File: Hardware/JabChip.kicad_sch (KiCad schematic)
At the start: 44 parts, among them J1 USB_C, J2 JSTPH, J3 Piezo+, J4 Piezo-, SW1 434133025816, SW2 434133025816, U1 AP2112K-3.3, U2 MCP73831-2-OT, U3 LSM6DS3, U4 ESP32-S3-WROOM-1

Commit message: style: Clean up schematic
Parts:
- D4: value LED -> LED_R
- D7: value LED -> LED_G
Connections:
- net +5V: now also C3.2; no longer C3.1
- net GND: now also C3.1; no longer C3.2
- no-connect marks 10 -> 8
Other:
- note added: "SENSORS"
- note removed: "IMU"
- moved on the sheet: C13, C3, J3, J4, R10, R11, R12, U3

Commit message: fix: Reassign piezo from IO3 to IO9 to avoid JTAG debug
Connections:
- net 9 is gone; now on net Piezo: U4.17 (IO9)
- net Piezo: no longer U4.15 (IO3)
- new net 3: U4.15 (IO3)
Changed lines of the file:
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@@
+		)
+	)
+	(global_label "Piezo"
+		(shape input)
+		(at 35.56 132.08 180)
+		(fields_autoplaced yes)
+		(effects
+			(font
+				(size 1.27 1.27)
+			)
+			(justify right)
+		)
+		(property "Intersheetrefs" "${INTERSHEET_REFS}"
+			(at 27.4343 132.08 0)
+			(effects
+				(font
+					(size 1.27 1.27)
+				)
+				(justify right)
+				(hide yes)
+			)
 		)
 	)
@@
 				(hide yes)
 			)
-		)
-	)
-	(global_label "Piezo"
-		(shape input)
-		(at 35.56 116.84 180)
-		(fields_autoplaced yes)
-		(effects
-			(font
-				(size 1.27 1.27)
-			)
-			(justify right)
-		)
-		(property "Intersheetrefs" "${INTERSHEET_REFS}"
-			(at 27.4343 116.84 0)
-			(effects
-				(font
-					(size 1.27 1.27)
-				)
-				(justify right)
-				(hide yes)
-			)

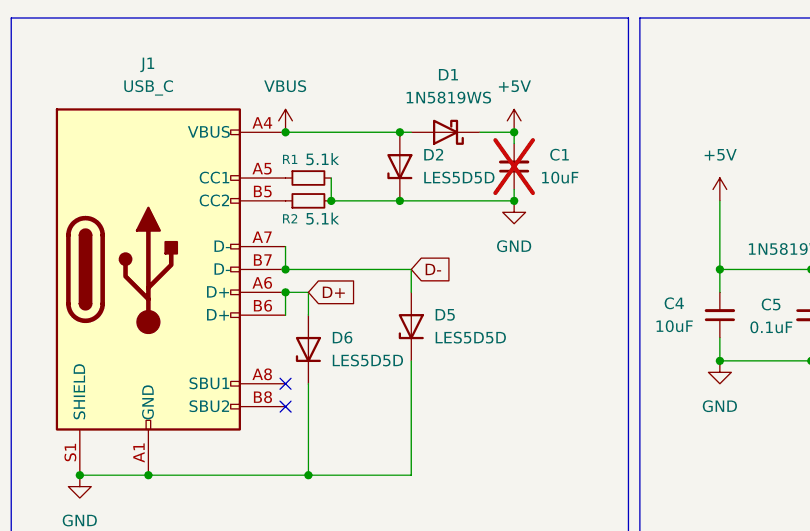
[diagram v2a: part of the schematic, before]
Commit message: !fix: Correct ESD protection diodes and regenerate gerber output files
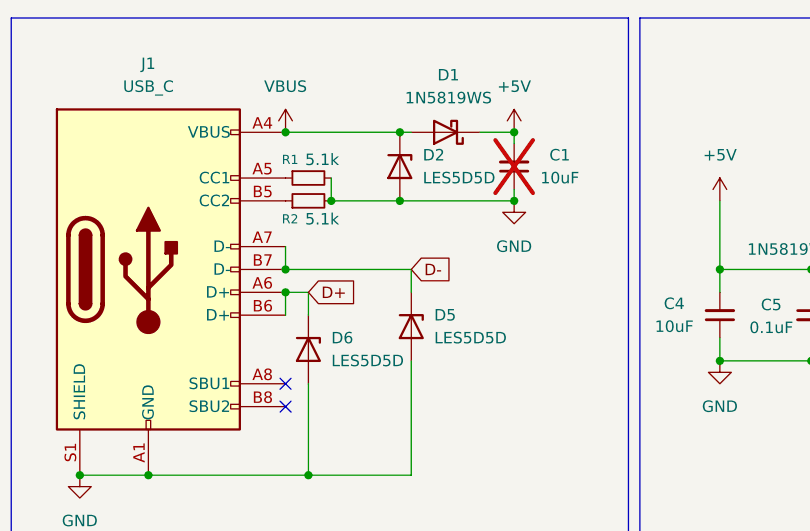
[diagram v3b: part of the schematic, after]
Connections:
- net D+: now also D6.1 (K); no longer D6.2 (A)
- net D-: now also D5.1 (K); no longer D5.2 (A)
- net GND: now also D2.2 (A), D5.2 (A), D6.2 (A); no longer D2.1 (K), D5.1 (K), D6.1 (K)
- net VBUS: now also D2.1 (K); no longer D2.2 (A)
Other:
- moved on the sheet: D2, D5, D6
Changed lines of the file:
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@@
 	)
 	(junction
+		(at 57.15 34.29)
+		(diameter 0)
+		(color 0 0 0 0)
+	)
+	(junction
 		(at 104.14 140.97)
 		(diameter 0)
@@
 	)
 	(junction
-		(at 57.15 26.67)
-		(diameter 0)
-		(color 0 0 0 0)
-	)
-	(junction
 		(at 194.31 147.32)
 		(diameter 0)
@@
 	)
 	(junction
-		(at 176.53 113.03)
+		(at 57.15 26.67)
 		(diameter 0)
 		(color 0 0 0 0)
 	)
 	(junction
-		(at 157.48 54.61)
+		(at 176.53 113.03)
 		(diameter 0)
 		(color 0 0 0 0)
 	)
 	(junction
-		(at 194.31 142.24)
+		(at 157.48 54.61)
 		(diameter 0)
 		(color 0 0 0 0)
 	)
 	(junction
-		(at 44.45 44.45)
+		(at 194.31 142.24)
 		(diameter 0)
 		(color 0 0 0 0)
 	)
 	(junction
-		(at 57.15 34.29)
+		(at 44.45 44.45)
 		(diameter 0)
 		(color 0 0 0 0)
@@
 	(wire
 		(pts
-			(xy 69.85 34.29) (xy 57.15 34.29)
+			(xy 57.15 26.67) (xy 58.42 26.67)
 		)
 		(stroke
@@
 	(wire
 		(pts
-			(xy 58.42 26.67) (xy 57.15 26.67)
+			(xy 114.3 111.76) (xy 120.65 111.76)
 		)
 		(stroke
@@
 	(wire
 		(pts
-			(xy 114.3 111.76) (xy 120.65 111.76)
+			(xy 76.2 119.38) (xy 71.12 119.38)
 		)
 		(stroke
@@
 	(wire
 		(pts
-			(xy 76.2 119.38) (xy 71.12 119.38)
+			(xy 104.14 127) (xy 104.14 140.97)
 		)
 		(stroke
@@
 	(wire
 		(pts
-			(xy 104.14 127) (xy 104.14 140.97)
+			(xy 109.22 111.76) (xy 114.3 111.76)
 		)
 		(stroke
@@
 	(wire
 		(pts
-			(xy 109.22 111.76) (xy 114.3 111.76)
+			(xy 35.56 121.92) (xy 40.64 121.92)
 		)
 		(stroke
@@
 	(wire
 		(pts
-			(xy 35.56 121.92) (xy 40.64 121.92)
+			(xy 57.15 34.29) (xy 69.85 34.29)
 		)
 		(stroke
@@
 	(symbol
 		(lib_id "Diode:ESD5Zxx")
-		(at 46.99 50.8 90)
+		(at 46.99 50.8 270)
 		(unit 1)
 		(exclude_from_sim no)
@@
 					(size 1.27 1.27)
 				)
-				(justify right)
+				(justify left)
 			)
 		)
@@
 					(size 1.27 1.27)
 				)
-				(justify right)
+				(justify left)
 			)
 		)
 		(property "Footprint" "Diode_SMD:D_SOD-523"
-			(at 51.435 50.8 0)
+			(at 42.545 50.8 0)
 			(effects
 				(font
@@
 	(symbol
 		(lib_id "Diode:ESD5Zxx")
-		(at 57.15 30.48 90)
+		(at 57.15 30.48 270)
 		(unit 1)
 		(exclude_from_sim no)
@@
 					(size 1.27 1.27)
 				)
-				(justify right)
+				(justify left)
 			)
 		)
@@
 					(size 1.27 1.27)
 				)
-				(justify right)
+				(justify left)
 			)
 		)
 		(property "Footprint" "Diode_SMD:D_SOD-523"
-			(at 61.595 30.48 0)
+			(at 52.705 30.48 0)
 			(effects
 				(font
@@
 	(symbol
 		(lib_id "Diode:ESD5Zxx")
-		(at 58.42 48.26 90)
+		(at 58.42 48.26 270)
 		(unit 1)
 		(exclude_from_sim no)
@@
 					(size 1.27 1.27)
 				)
-				(justify right)
+				(justify left)
 			)
 		)
@@
 					(size 1.27 1.27)
 				)
-				(justify right)
+				(justify left)
 			)
 		)
 		(property "Footprint" "Diode_SMD:D_SOD-523"
-			(at 62.865 48.26 0)
+			(at 53.975 48.26 0)
 			(effects
 				(font
